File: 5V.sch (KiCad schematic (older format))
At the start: 37 parts, among them U16 TPS61088, U17 TPS61088

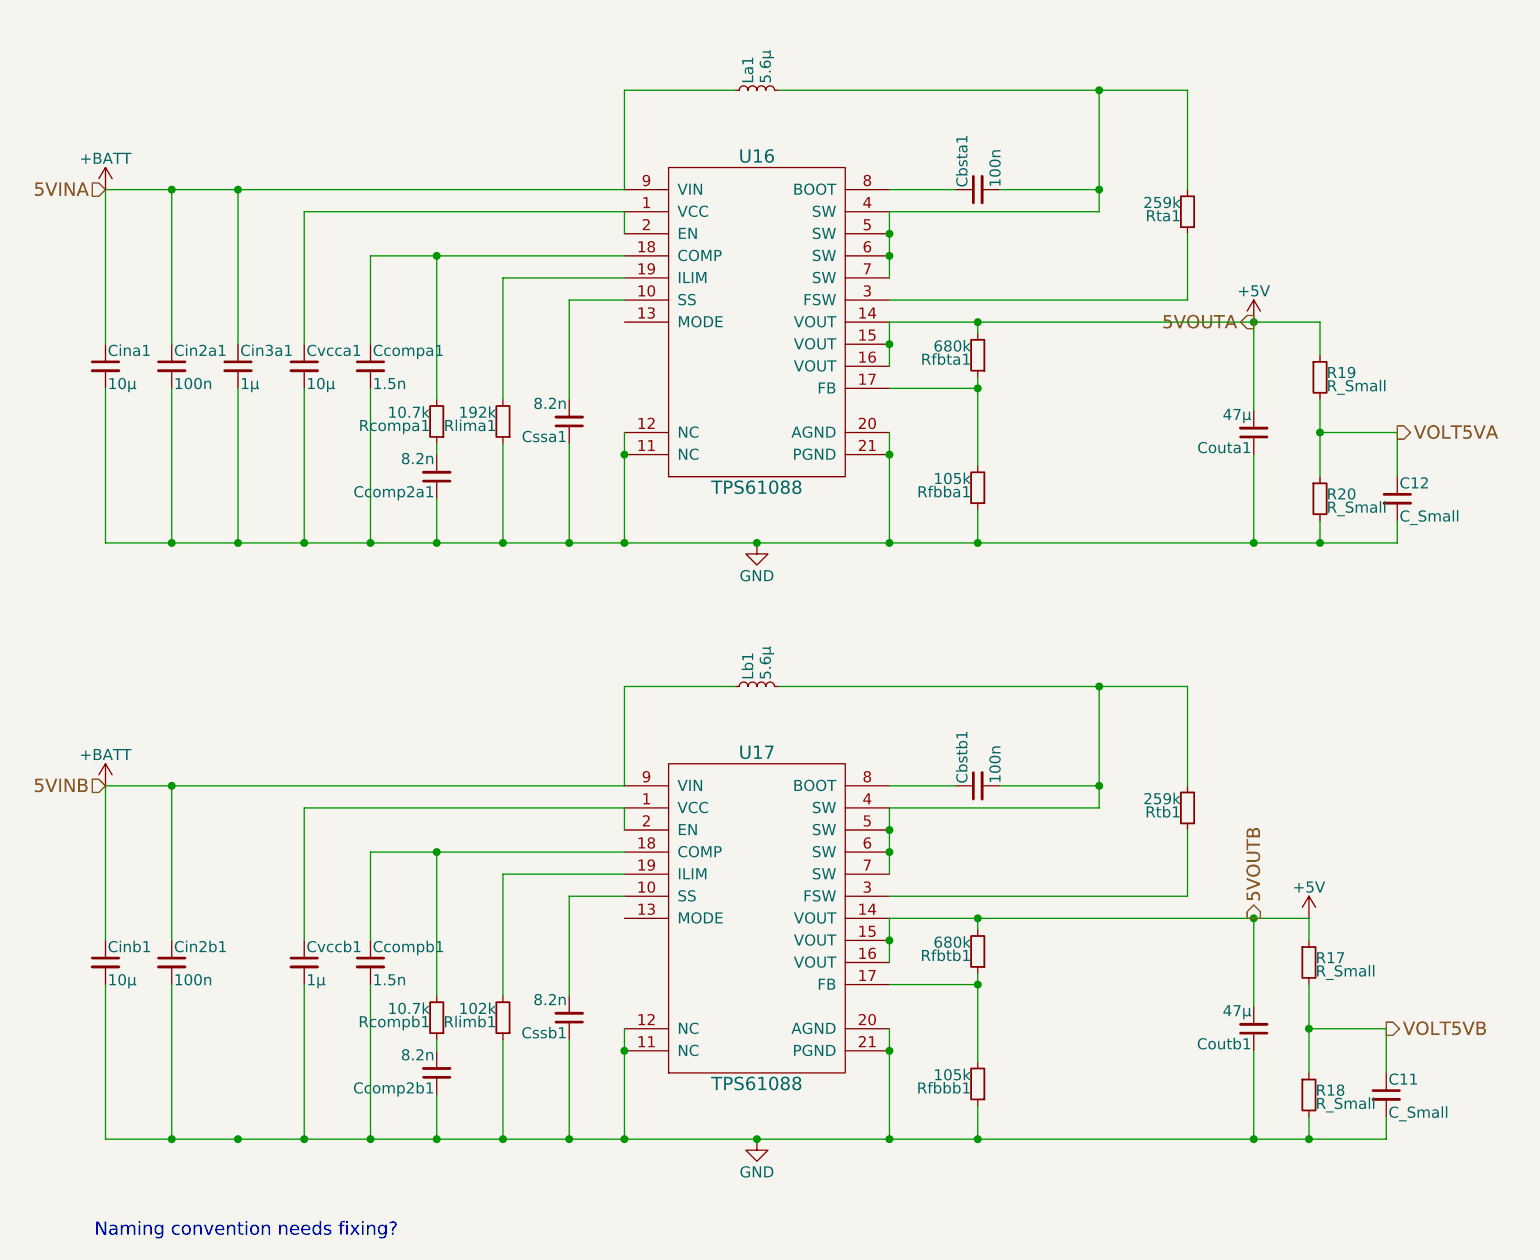
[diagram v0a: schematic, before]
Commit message: PCB layout as of 2018-02-12
All that’s left to do is add deployment switches
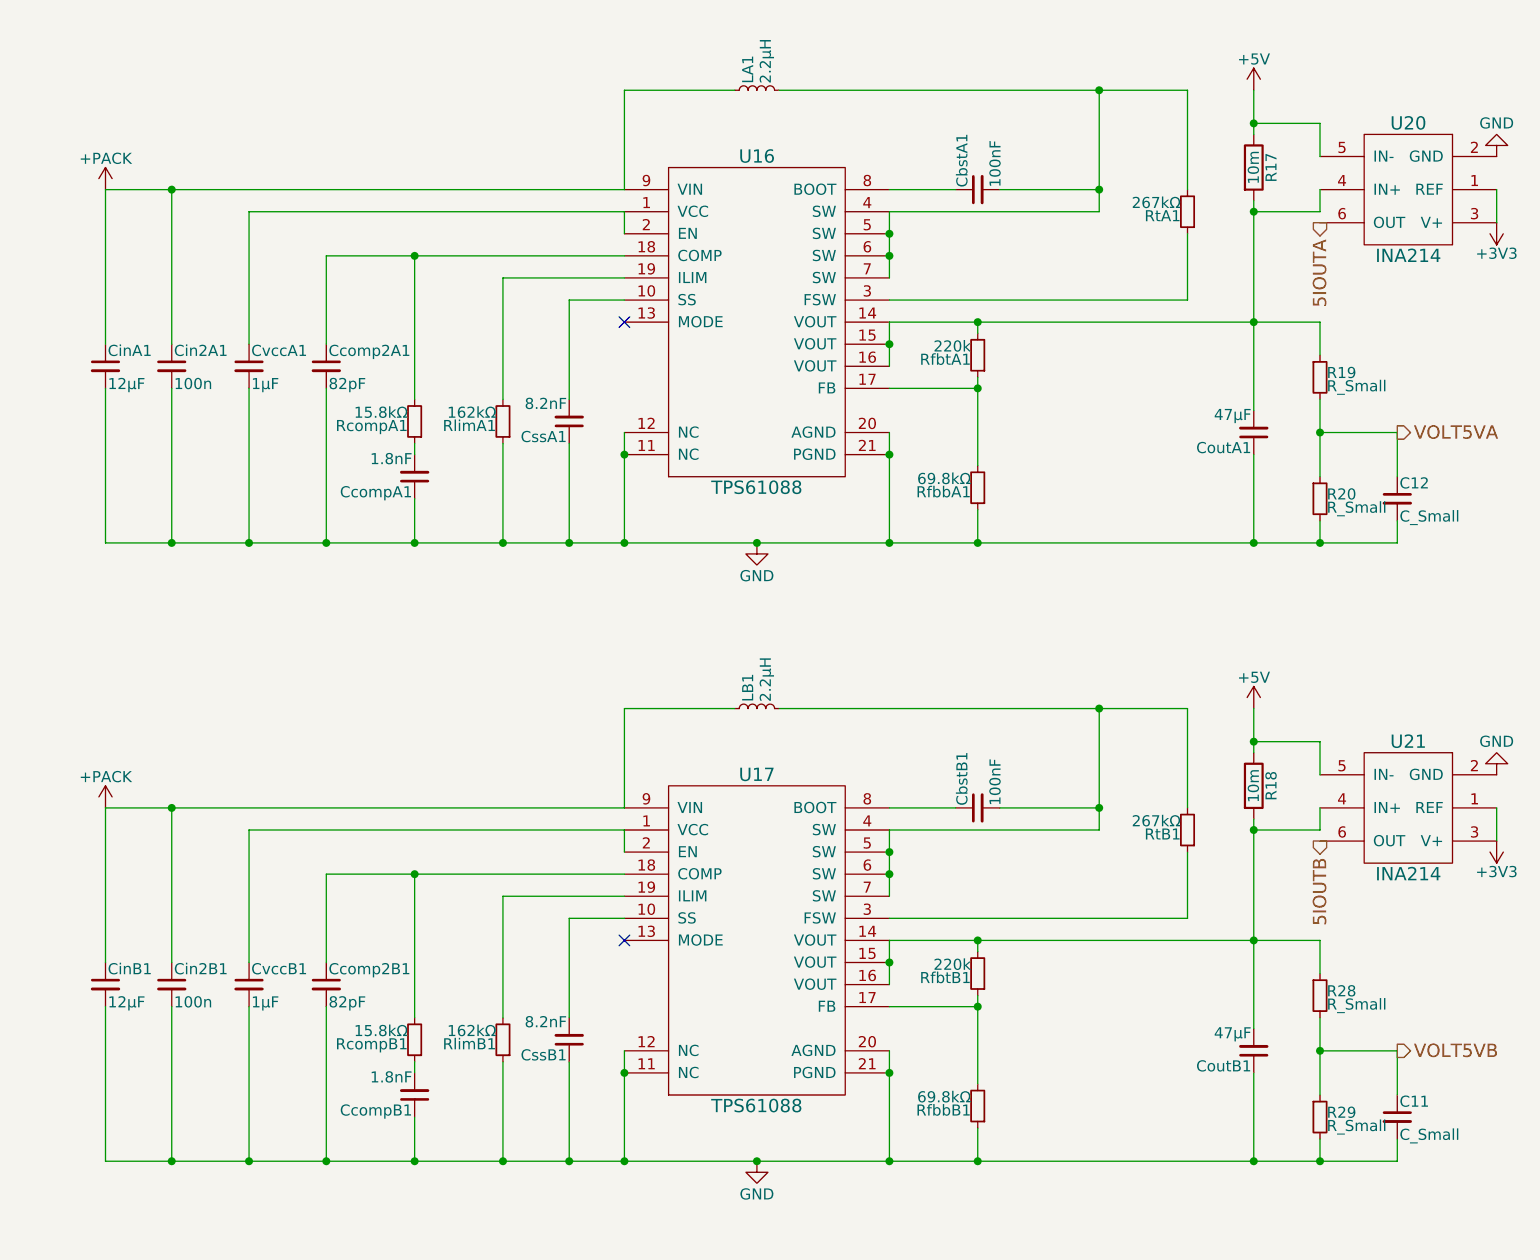
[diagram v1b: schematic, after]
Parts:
- removed Cbstb1, Cin2b1: 100n, symbol C_Small
- removed Ccomp2b1, Cssb1: 8.2n, symbol C_Small
- removed Ccompb1: 1.5n, symbol C_Small
- removed Cin3a1, Cvccb1: 1µ, symbol C_Small
- removed Cinb1: 10µ, symbol C_Small
- removed Coutb1: 47µ, symbol C_Small
- removed Lb1: 5.6µ, symbol L_Small
- removed R17, R18: R_Small, symbol R_Small
- removed Rcompb1: 10.7k, symbol R_Small
- removed Rfbbb1: 105k, symbol R_Small
- removed Rfbtb1: 680k, symbol R_Small
- removed Rlimb1: 102k, symbol R_Small
- removed Rtb1: 259k, symbol R_Small
- added CbstB1: 100nF, Capacitors_SMD:C_0603_HandSoldering, symbol C_Small
- added Ccomp2B1: 82pF, Capacitors_SMD:C_0603_HandSoldering, symbol C_Small
- added CcompB1: 1.8nF, Capacitors_SMD:C_0603_HandSoldering, symbol C_Small
- added Cin2B1: 100n, Capacitors_SMD:C_0603_HandSoldering, symbol C_Small
- added CinB1: 12µF, Capacitors_SMD:C_0603_HandSoldering, symbol C_Small
- added CoutB1: 47µF, Capacitors_SMD:C_0603_HandSoldering, symbol C_Small
- added CssB1: 8.2nF, Capacitors_SMD:C_0603_HandSoldering, symbol C_Small
- added CvccB1: 1µF, Capacitors_SMD:C_0603_HandSoldering, symbol C_Small
- added LB1: 2.2µH, eps-libraries:SRN8040, symbol L_Small
- added R17, R18: 10m, Resistors_SMD:R_0603_HandSoldering, symbol R
- added R28, R29: R_Small, Resistors_SMD:R_0603_HandSoldering, symbol R_Small
- added RcompB1: 15.8kΩ, Resistors_SMD:R_0603_HandSoldering, symbol R_Small
- added RfbbB1: 69.8kΩ, Resistors_SMD:R_0603_HandSoldering, symbol R_Small
- added RfbtB1: 220k, Resistors_SMD:R_0603_HandSoldering, symbol R_Small
- added RlimB1: 162kΩ, Resistors_SMD:R_0603_HandSoldering, symbol R_Small
- added RtB1: 267kΩ, Resistors_SMD:R_0603_HandSoldering, symbol R_Small
- added U20, U21: INA214, kicad-libraries:SC70-6, symbol INA214
- C11, C12: footprint (none) -> Capacitors_SMD:C_0603_HandSoldering
- CbstA1: renamed from Cbsta1; value 100n -> 100nF; footprint (none) -> Capacitors_SMD:C_0603_HandSoldering
- Ccomp2A1: renamed from Ccompa1; value 1.5n -> 82pF; footprint (none) -> Capacitors_SMD:C_0603_HandSoldering
- CcompA1: renamed from Ccomp2a1; value 8.2n -> 1.8nF; footprint (none) -> Capacitors_SMD:C_0603_HandSoldering
- Cin2A1: renamed from Cin2a1; footprint (none) -> Capacitors_SMD:C_0603_HandSoldering
- CinA1: renamed from Cina1; value 10µ -> 12µF; footprint (none) -> Capacitors_SMD:C_0603_HandSoldering
- CoutA1: renamed from Couta1; value 47µ -> 47µF; footprint (none) -> Capacitors_SMD:C_0603_HandSoldering
- CssA1: renamed from Cssa1; value 8.2n -> 8.2nF; footprint (none) -> Capacitors_SMD:C_0603_HandSoldering
- CvccA1: renamed from Cvcca1; value 10µ -> 1µF; footprint (none) -> Capacitors_SMD:C_0603_HandSoldering
- LA1: renamed from La1; value 5.6µ -> 2.2µH; footprint (none) -> eps-libraries:SRN8040
- R19, R20: footprint (none) -> Resistors_SMD:R_0603_HandSoldering
- RcompA1: renamed from Rcompa1; value 10.7k -> 15.8kΩ; footprint (none) -> Resistors_SMD:R_0603_HandSoldering
- RfbbA1: renamed from Rfbba1; value 105k -> 69.8kΩ; footprint (none) -> Resistors_SMD:R_0603_HandSoldering
- RfbtA1: renamed from Rfbta1; value 680k -> 220k; footprint (none) -> Resistors_SMD:R_0603_HandSoldering
- RlimA1: renamed from Rlima1; value 192k -> 162kΩ; footprint (none) -> Resistors_SMD:R_0603_HandSoldering
- RtA1: renamed from Rta1; value 259k -> 267kΩ; footprint (none) -> Resistors_SMD:R_0603_HandSoldering
- U16, U17: footprint (none) -> w_smd_qfn:pvqfn-n20
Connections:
- net +5V: now also R17.1, R18.1, U20.5 (IN-), U21.5 (IN-); no longer CoutA1.2, R19.1, RfbtA1.2, U16.14 (VOUT), U16.15 (VOUT), U16.16 (VOUT), U17.14 (VOUT), U17.15 (VOUT), U17.16 (VOUT)
- net GND: now also Ccomp2B1.2, CcompB1.1, Cin2B1.2, CinB1.2, CoutB1.1, CssB1.1, CvccB1.2, R29.2, RfbbB1.1, RlimB1.1, U20.2 (GND), U21.2 (GND)
- net VOLT5VB: now also R28.2, R29.1
- net at U17.1 (VCC), U17.2 (EN): now also CvccB1.1
- net at U17.10 (SS): now also CssB1.2
- net at U17.17 (FB): now also RfbbB1.2, RfbtB1.1
- net at U17.18 (COMP): now also Ccomp2B1.1, RcompB1.2
- net at U17.19 (ILIM): now also RlimB1.2
- net at U17.3 (FSW): now also RtB1.1
- net at U17.4 (SW), U17.5 (SW), U17.6 (SW)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: now also CbstB1.2, LB1.2, RtB1.2
- net at U17.8 (BOOT): now also CbstB1.1
- net +BATT renamed +PACK
- net +PACK: now also Cin2B1.1, CinB1.1, LB1.1
- new net: CoutA1.2, R17.2, R19.1, RfbtA1.2, U16.14 (VOUT), U16.15 (VOUT), U16.16 (VOUT), U20.4 (IN+)
- new net: CoutB1.2, R18.2, R28.1, RfbtB1.2, U17.14 (VOUT), U17.15 (VOUT), U17.16 (VOUT), U21.4 (IN+)
- new net: CcompB1.2, RcompB1.1
- new net +3V3: U20.1 (REF), U20.3 (V+), U21.1 (REF), U21.3 (V+)
- new net 5IOUTA: U20.6 (OUT)
- new net 5IOUTB: U21.6 (OUT)
- no-connect marks 0 -> 2
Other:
- note removed: "Naming convention needs fixing?"
- moved on the sheet: Ccomp2A1, CcompA1, CvccA1, RcompA1
